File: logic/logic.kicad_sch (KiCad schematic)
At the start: 24 parts, among them J1 DIN41612_03x32_ABC, U1 TPIC6595, U2 TPIC6595, U3 TPIC6595, U4 TPIC6595, U5 TPIC6595, U6 TPIC6595, U7 TPIC6595, U8 TPIC6595, U9 74HC14

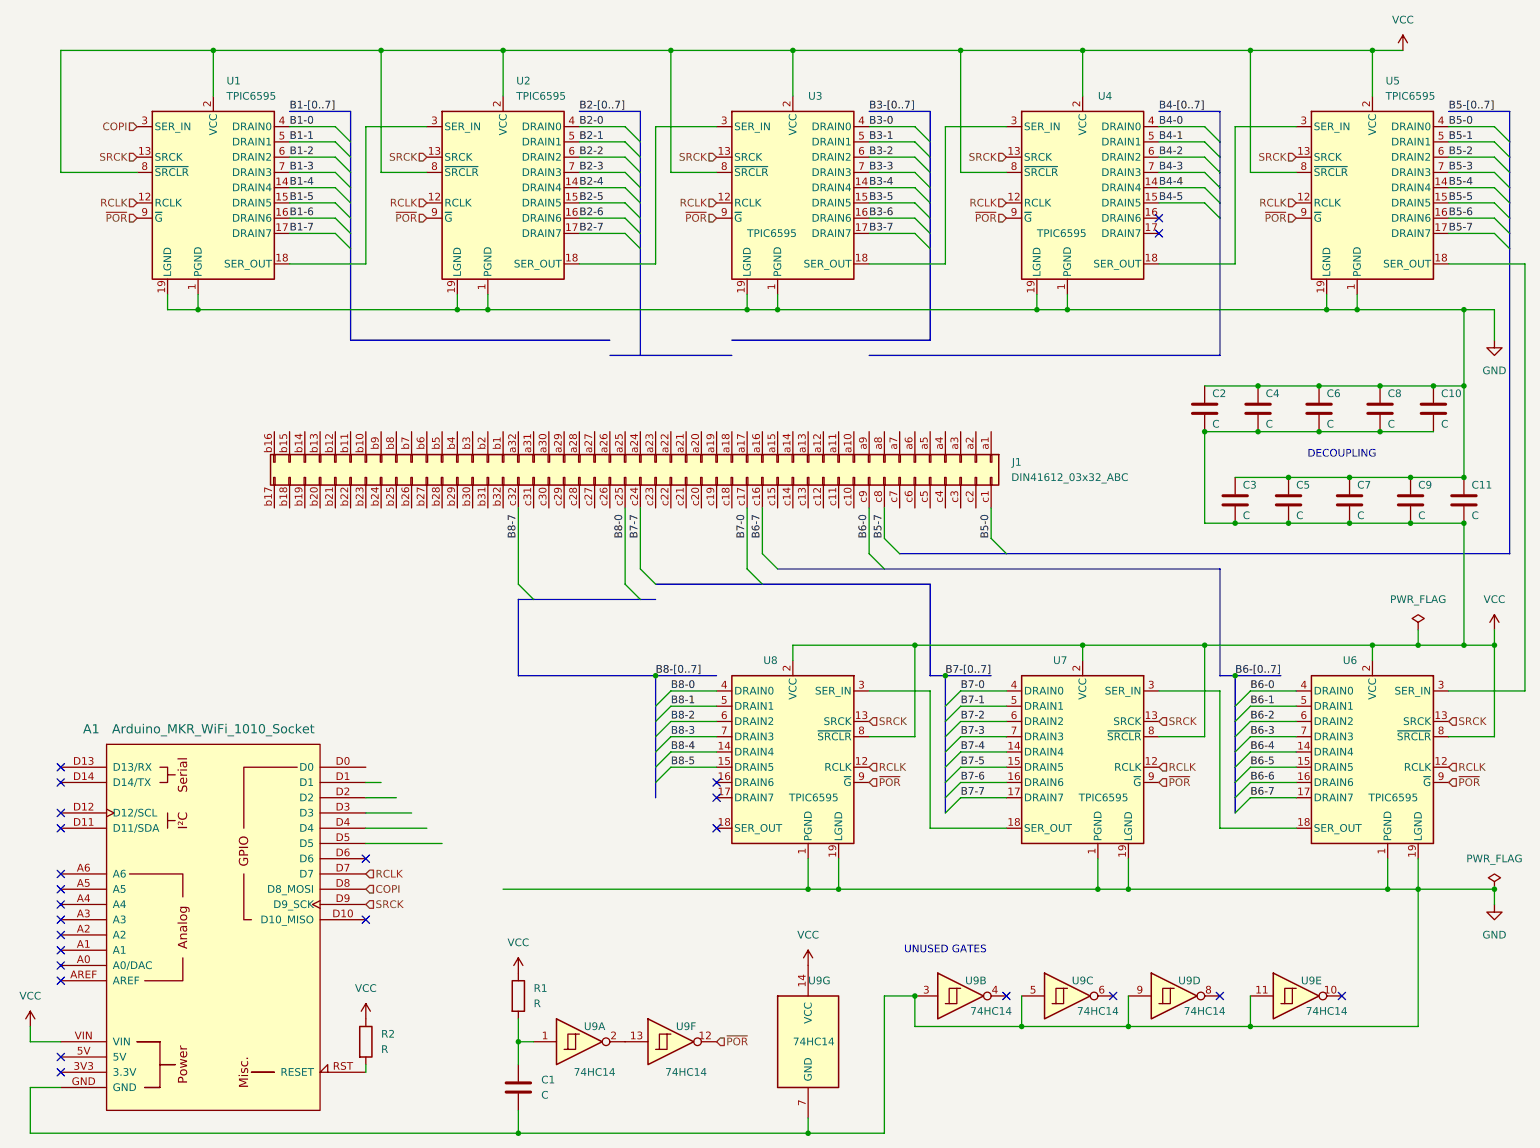
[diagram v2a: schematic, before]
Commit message: Complete schematic. No DRC errors. Place components on PCB.
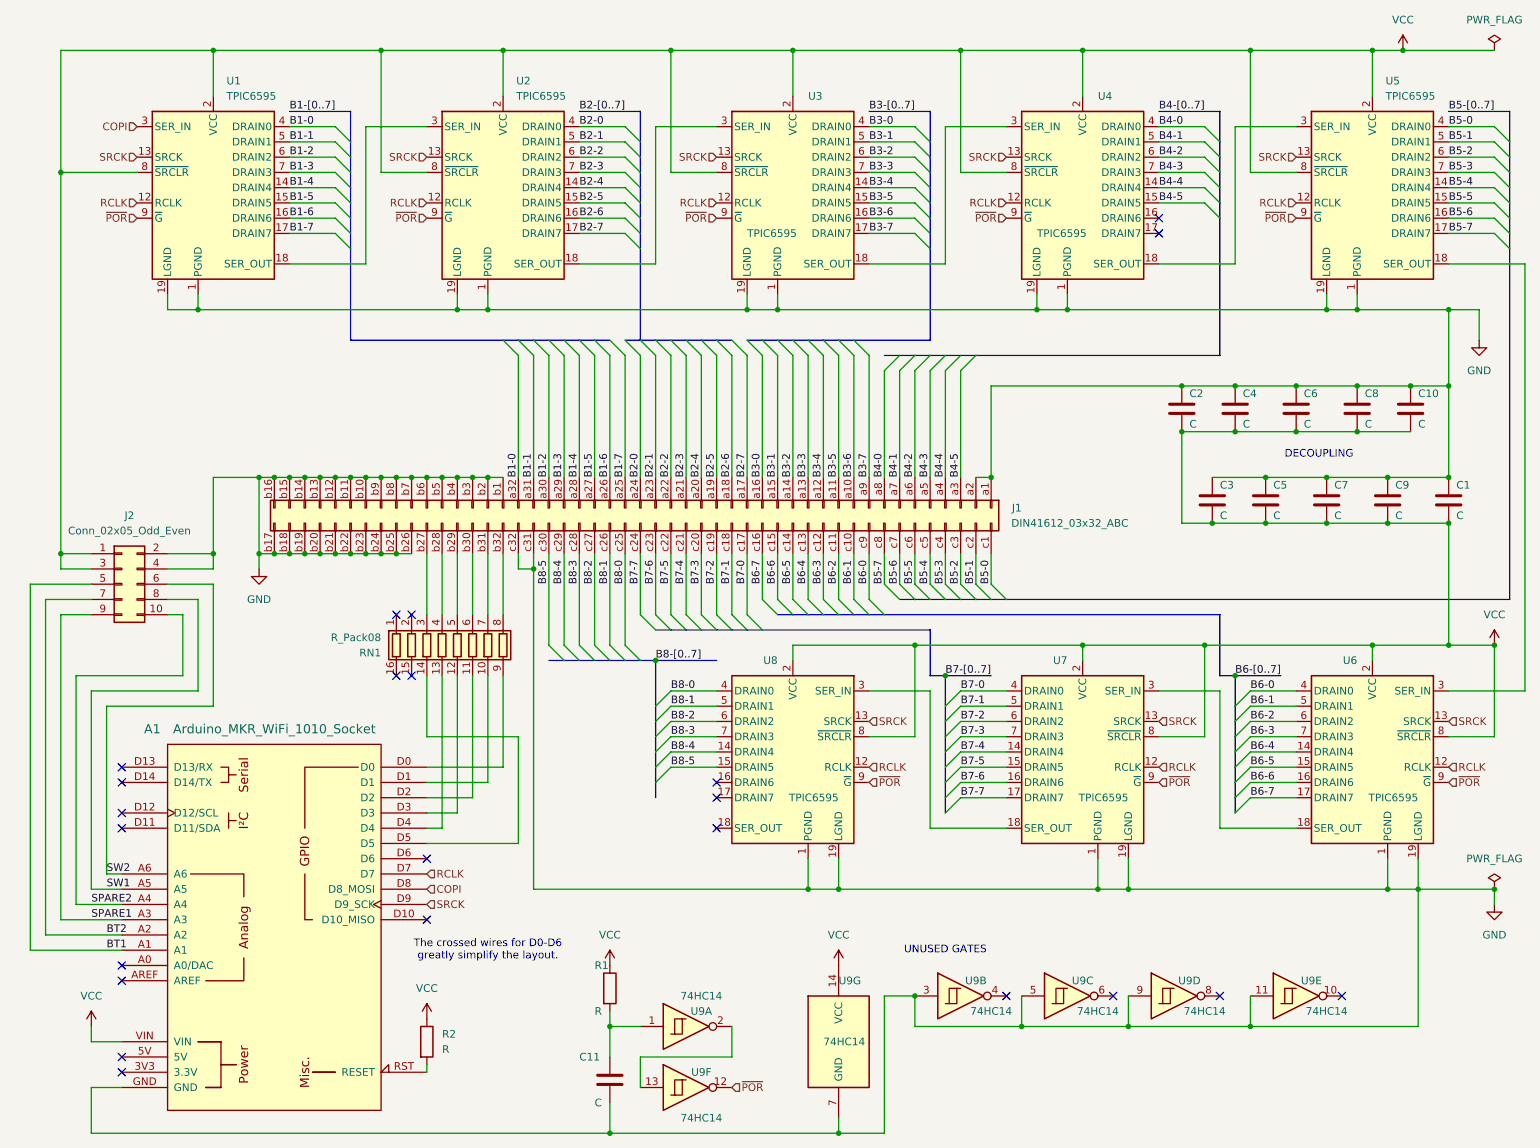
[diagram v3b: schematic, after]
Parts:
- removed C1: C, symbol Device:C
- added C11: C, Capacitor_THT:CP_Radial_D8.0mm_P2.50mm, symbol Device:C
- added J2: Conn_02x05_Odd_Even, Connector_PinHeader_2.54mm:PinHeader_2x05_P2.54mm_Vertical, symbol Connector_Generic:Conn_02x05_Odd_Even
- added RN1: R_Pack08, Package_DIP:DIP-16_W7.62mm_Socket, symbol Device:R_Pack08
- A1: footprint PCM_arduino-library:Arduino_MKR_WiFi_1010_Socket -> arduino-library:Arduino_MKR_WiFi_1010_Socket
- C1: renamed from C11; footprint (none) -> Capacitor_THT:C_Disc_D3.4mm_W2.1mm_P2.50mm
- C10, C2, C3, C4, C5, C6, C7, C8, C9: footprint (none) -> Capacitor_THT:C_Disc_D3.4mm_W2.1mm_P2.50mm
- J1: footprint (none) -> Connector_DIN:DIN41612_R_3x32_Male_Vertical_THT
- R1, R2: footprint (none) -> Resistor_THT:R_Axial_DIN0207_L6.3mm_D2.5mm_P10.16mm_Horizontal
- U2, U3, U4, U5, U6, U7, U8: footprint (none) -> Package_DIP:DIP-20_W7.62mm_Socket
- U9: footprint (none) -> Package_DIP:DIP-14_W7.62mm_Socket
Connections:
- net B8-7 is gone; now on net GND: J1.c32 (Pin_c32)
- net B1-0: now also J1.a32 (Pin_a32)
- net B1-1: now also J1.a31 (Pin_a31)
- net B1-2: now also J1.a30 (Pin_a30)
- net B1-3: now also J1.a29 (Pin_a29)
- net B1-4: now also J1.a28 (Pin_a28)
- net B1-5: now also J1.a27 (Pin_a27)
- net B1-6: now also J1.a26 (Pin_a26)
- net B1-7: now also J1.a25 (Pin_a25)
- net B2-0: now also J1.a24 (Pin_a24)
- net B2-1: now also J1.a23 (Pin_a23)
- net B2-2: now also J1.a22 (Pin_a22)
- net B2-3: now also J1.a21 (Pin_a21)
- net B2-4: now also J1.a20 (Pin_a20)
- net B2-5: now also J1.a19 (Pin_a19)
- net B2-6: now also J1.a18 (Pin_a18)
- net B2-7: now also J1.a17 (Pin_a17)
- net B3-0: now also J1.a16 (Pin_a16)
- net B3-1: now also J1.a15 (Pin_a15)
- net B3-2: now also J1.a14 (Pin_a14)
- net B3-3: now also J1.a13 (Pin_a13)
- net B3-4: now also J1.a12 (Pin_a12)
- net B3-5: now also J1.a11 (Pin_a11)
- net B3-6: now also J1.a10 (Pin_a10)
- net B3-7: now also J1.a9 (Pin_a9)
- net B4-0: now also J1.a8 (Pin_a8)
- net B4-1: now also J1.a7 (Pin_a7)
- net B4-2: now also J1.a6 (Pin_a6)
- net B4-3: now also J1.a5 (Pin_a5)
- net B4-4: now also J1.a4 (Pin_a4)
- net B4-5: now also J1.a3 (Pin_a3)
- net B5-1: now also J1.c2 (Pin_c2)
- net B5-2: now also J1.c3 (Pin_c3)
- net B5-3: now also J1.c4 (Pin_c4)
- net B5-4: now also J1.c5 (Pin_c5)
- net B5-5: now also J1.c6 (Pin_c6)
- net B5-6: now also J1.c7 (Pin_c7)
- net B6-1: now also J1.c10 (Pin_c10)
- net B6-2: now also J1.c11 (Pin_c11)
- net B6-3: now also J1.c12 (Pin_c12)
- net B6-4: now also J1.c13 (Pin_c13)
- net B6-5: now also J1.c14 (Pin_c14)
- net B6-6: now also J1.c15 (Pin_c15)
- net B7-1: now also J1.c18 (Pin_c18)
- net B7-2: now also J1.c19 (Pin_c19)
- net B7-3: now also J1.c20 (Pin_c20)
- net B7-4: now also J1.c21 (Pin_c21)
- net B7-5: now also J1.c22 (Pin_c22)
- net B7-6: now also J1.c23 (Pin_c23)
- net B8-1: now also J1.c26 (Pin_c26)
- net B8-2: now also J1.c27 (Pin_c27)
- net B8-3: now also J1.c28 (Pin_c28)
- net B8-4: now also J1.c29 (Pin_c29)
- net B8-5: now also J1.c30 (Pin_c30)
- net GND: now also J1.a1 (Pin_a1), J1.a2 (Pin_a2), J1.b1 (Pin_b1), J1.b10 (Pin_b10), J1.b11 (Pin_b11), J1.b12 (Pin_b12), J1.b13 (Pin_b13), J1.b14 (Pin_b14), J1.b15 (Pin_b15), J1.b16 (Pin_b16), J1.b17 (Pin_b17), J1.b18 (Pin_b18), J1.b19 (Pin_b19), J1.b2 (Pin_b2), J1.b20 (Pin_b20), J1.b21 (Pin_b21), J1.b22 (Pin_b22), J1.b23 (Pin_b23), J1.b24 (Pin_b24), J1.b25 (Pin_b25), J1.b26 (Pin_b26), J1.b3 (Pin_b3), J1.b4 (Pin_b4), J1.b5 (Pin_b5), J1.b6 (Pin_b6), J1.b7 (Pin_b7), J1.b8 (Pin_b8), J1.b9 (Pin_b9), J1.c31 (Pin_c31), C11.2, J2.2 (Pin_2), J2.4 (Pin_4)
- net VCC: now also J2.1 (Pin_1), J2.3 (Pin_3)
- net at R1.2, U9.1: now also C11.1
- net BT1: now reaches A1.A1
- net BT1: now also J2.5 (Pin_5)
- net BT2: now reaches A1.A2
- net BT2: now also J2.7 (Pin_7)
- net SPARE1: now reaches A1.A3
- net SPARE1: now also J2.9 (Pin_9)
- net SPARE2: now reaches A1.A4
- net SPARE2: now also J2.10 (Pin_10)
- net SW1: now reaches A1.A5
- net SW1: now also J2.8 (Pin_8)
- net SW2: now reaches A1.A6
- net SW2: now also J2.6 (Pin_6)
- net at A1.D0: now also RN1.9 (R8.2)
- net at A1.D1: now also RN1.10 (R7.2)
- net at A1.D2: now also RN1.11 (R6.2)
- net at A1.D3: now also RN1.12 (R5.2)
- net at A1.D4: now also RN1.13 (R4.2)
- net at A1.D5: now also RN1.14 (R3.2)
- net at J1.b27 (Pin_b27): now also RN1.3 (R3.1)
- net at J1.b28 (Pin_b28): now also RN1.4 (R4.1)
- net at J1.b29 (Pin_b29): now also RN1.5 (R5.1)
- net at J1.b30 (Pin_b30): now also RN1.6 (R6.1)
- net at J1.b31 (Pin_b31): now also RN1.7 (R7.1)
- net at J1.b32 (Pin_b32): now also RN1.8 (R8.1)
- no-connect marks 25 -> 23
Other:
- note added: "The crossed wires for D0-D6 greatly simplify the layout."
- moved on the sheet: A1, C1, C10, C2, C3, C4, C5, C6, C7, C8, C9, J1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

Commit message: Add footprint for HV supply to NixComp library and schematic.
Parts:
- added S1: ~, symbol NixComp:NCH8200HV_170v
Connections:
- net GND: now also S1.2 (LVGND), S1.3 (PGND); no longer J1.b1 (Pin_b1), J1.b2 (Pin_b2), J1.b3 (Pin_b3), J1.b4 (Pin_b4), J1.b5 (Pin_b5), J1.b6 (Pin_b6), J1.b7 (Pin_b7)
- net VCC: now also S1.1 (LV_IN)
- new net: J1.b1 (Pin_b1), J1.b2 (Pin_b2), J1.b3 (Pin_b3), J1.b4 (Pin_b4), J1.b5 (Pin_b5), J1.b6 (Pin_b6), J1.b7 (Pin_b7), S1.4 (HV_OUT)
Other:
- moved on the sheet: J2

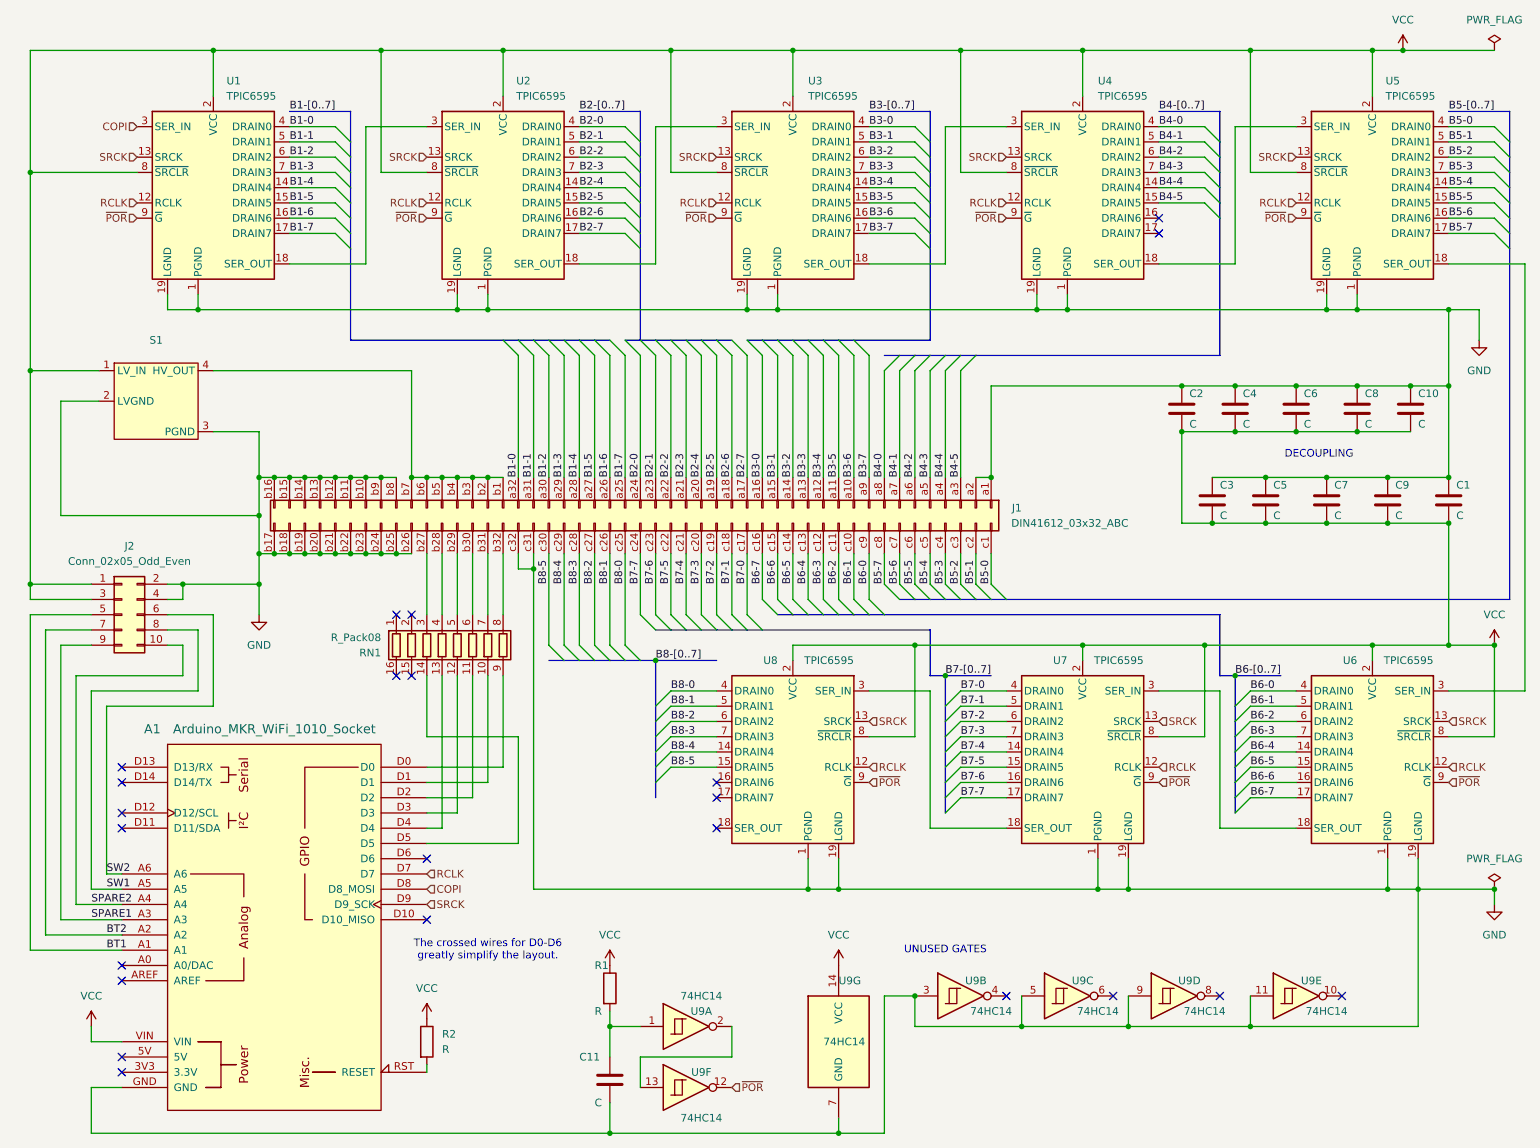
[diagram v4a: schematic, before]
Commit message: Some changes to logic board. Begin schematic for display board.
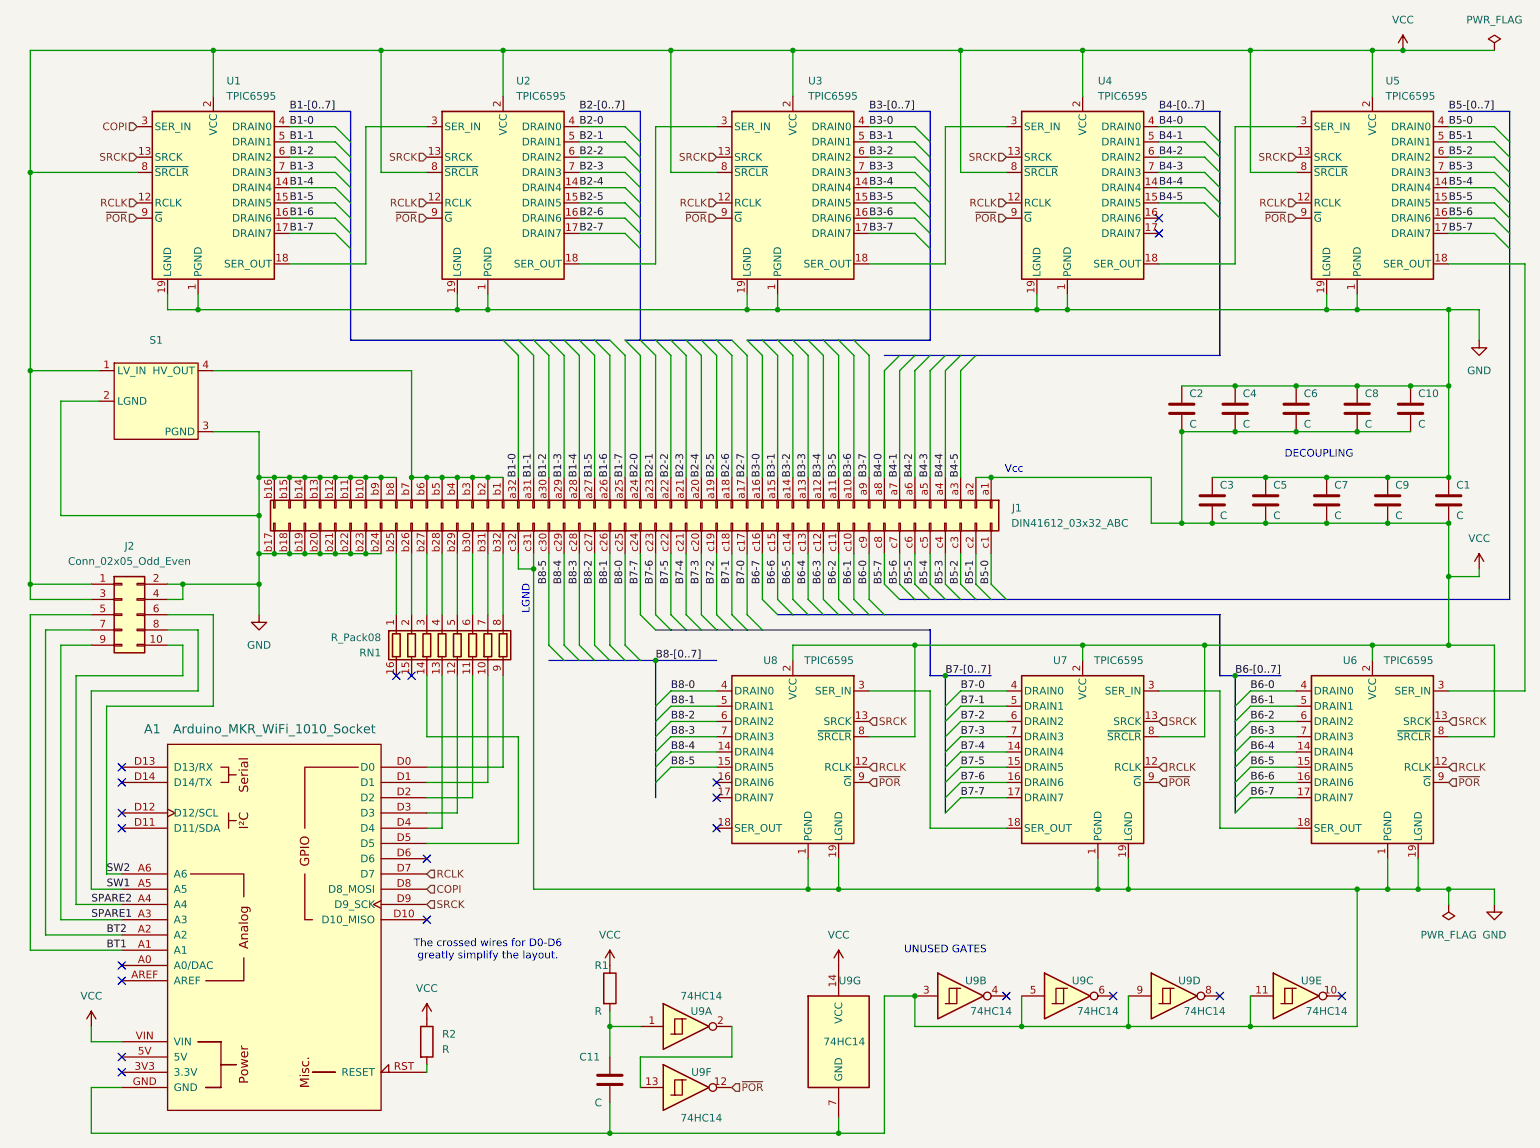
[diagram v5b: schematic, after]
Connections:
- net GND: no longer J1.a1 (Pin_a1), J1.a2 (Pin_a2), J1.b25 (Pin_b25), J1.b26 (Pin_b26)
- net VCC: now also J1.a1 (Pin_a1), J1.a2 (Pin_a2)
- net at RN1.1 (R1.1): now also J1.b25 (Pin_b25)
- net at RN1.2 (R2.1): now also J1.b26 (Pin_b26)
- no-connect marks 23 -> 21
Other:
- note added: "LGND"
- note added: "Vcc"

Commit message: Update schematic and PCB with HV supply footprint
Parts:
- S1: footprint (none) -> NixComp:NCH8200HV
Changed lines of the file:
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@@
 			)
 		)
-		(property "Footprint" ""
+		(property "Footprint" "NixComp:NCH8200HV"
 			(at 38.1 78.74 0)
 			(effects
